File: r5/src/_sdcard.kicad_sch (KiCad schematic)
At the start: 6 parts, among them J14 Micro_SD_Card_Det_JAE_ST11, U10 ESD7004, U11 ESD7004

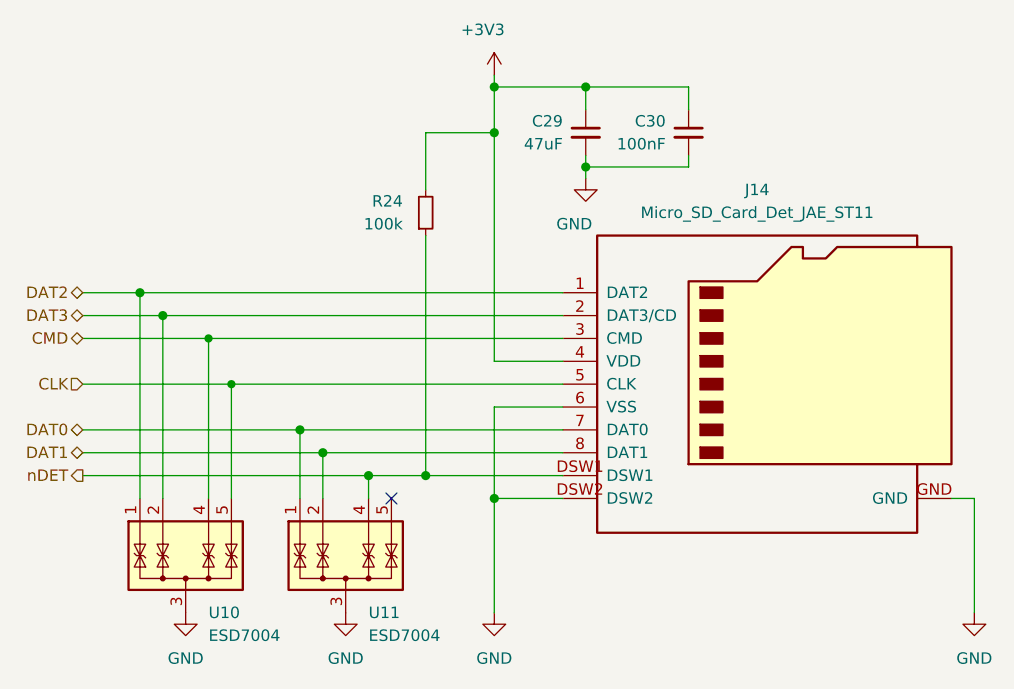
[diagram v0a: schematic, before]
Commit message: Updates to +/-15V supply. Additional output capacitance. Change to smaller inductor packages. Add 0R links to permit isolation of output. Mods to compensation network. Set feedback resistors to datasheet values.
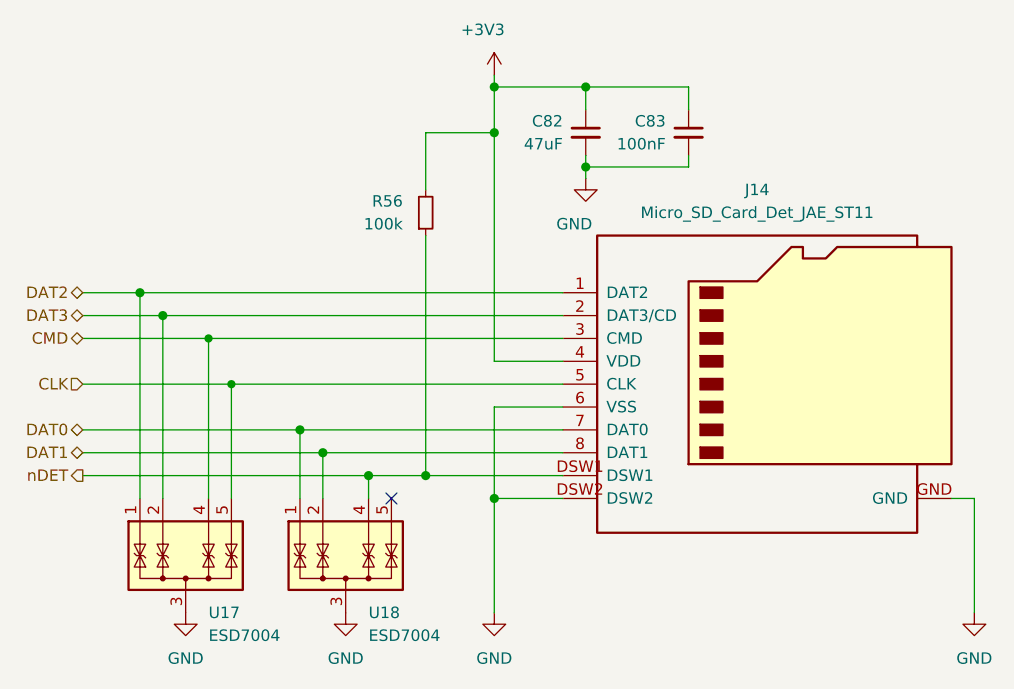
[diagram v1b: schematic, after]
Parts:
- renumbered C29 to C82, C30 to C83, R24 to R56, U10 to U17, U11 to U18
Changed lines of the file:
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@@
   (symbol (lib_id "power:GND") (at 152.4 128.27 0) (unit 1)
     (in_bom yes) (on_board yes) (dnp no)
-    (property "Reference" "#PWR089" (at 152.4 134.62 0)
+    (property "Reference" "#PWR0160" (at 152.4 134.62 0)
       (effects (font (size 1.27 1.27)) hide)
     )
@@
       (project "bugg-main-r5"
         (path "/e3eb514f-6ce4-4abe-ba20-f82f0015628f/498d2354-7ecc-4881-a4b8-afc4730b4589"
-          (reference "#PWR089") (unit 1)
+          (reference "#PWR0160") (unit 1)
         )
       )
@@
   (symbol (lib_id "Device:R_Small") (at 144.78 83.82 0) (mirror x) (unit 1)
     (in_bom yes) (on_board yes) (dnp no)
-    (property "Reference" "R24" (at 142.24 82.55 0)
+    (property "Reference" "R56" (at 142.24 82.55 0)
       (effects (font (size 1.27 1.27)) (justify right))
     )
@@
       (project "bugg-main-r5"
         (path "/e3eb514f-6ce4-4abe-ba20-f82f0015628f/498d2354-7ecc-4881-a4b8-afc4730b4589"
-          (reference "R24") (unit 1)
+          (reference "R56") (unit 1)
         )
       )
@@
   (symbol (lib_id "Device:C_Small") (at 173.99 74.93 0) (mirror y) (unit 1)
     (in_bom yes) (on_board yes) (dnp no)
-    (property "Reference" "C30" (at 171.45 73.66 0)
+    (property "Reference" "C83" (at 171.45 73.66 0)
       (effects (font (size 1.27 1.27)) (justify left))
     )
@@
       (project "bugg-main-r5"
         (path "/e3eb514f-6ce4-4abe-ba20-f82f0015628f/498d2354-7ecc-4881-a4b8-afc4730b4589"
-          (reference "C30") (unit 1)
+          (reference "C83") (unit 1)
         )
       )
@@
   (symbol (lib_id "power:GND") (at 205.74 128.27 0) (unit 1)
     (in_bom yes) (on_board yes) (dnp no)
-    (property "Reference" "#PWR091" (at 205.74 134.62 0)
+    (property "Reference" "#PWR0162" (at 205.74 134.62 0)
       (effects (font (size 1.27 1.27)) hide)
     )
@@
       (project "bugg-main-r5"
         (path "/e3eb514f-6ce4-4abe-ba20-f82f0015628f/498d2354-7ecc-4881-a4b8-afc4730b4589"
-          (reference "#PWR091") (unit 1)
+          (reference "#PWR0162") (unit 1)
         )
       )
@@
   (symbol (lib_id "Device:C_Small") (at 162.56 74.93 0) (mirror y) (unit 1)
     (in_bom yes) (on_board yes) (dnp no)
-    (property "Reference" "C29" (at 160.02 73.66 0)
+    (property "Reference" "C82" (at 160.02 73.66 0)
       (effects (font (size 1.27 1.27)) (justify left))
     )
@@
       (project "bugg-main-r5"
         (path "/e3eb514f-6ce4-4abe-ba20-f82f0015628f/498d2354-7ecc-4881-a4b8-afc4730b4589"
-          (reference "C29") (unit 1)
+          (reference "C82") (unit 1)
         )
       )
@@
   (symbol (lib_id "power:GND") (at 118.11 128.27 0) (unit 1)
     (in_bom yes) (on_board yes) (dnp no)
-    (property "Reference" "#PWR086" (at 118.11 134.62 0)
+    (property "Reference" "#PWR0157" (at 118.11 134.62 0)
       (effects (font (size 1.27 1.27)) hide)
     )
@@
       (project "bugg-main-r5"
         (path "/e3eb514f-6ce4-4abe-ba20-f82f0015628f/498d2354-7ecc-4881-a4b8-afc4730b4589"
-          (reference "#PWR086") (unit 1)
+          (reference "#PWR0157") (unit 1)
         )
       )
@@
   (symbol (lib_id "power:GND") (at 162.56 80.01 0) (mirror y) (unit 1)
     (in_bom yes) (on_board yes) (dnp no)
-    (property "Reference" "#PWR090" (at 162.56 86.36 0)
+    (property "Reference" "#PWR0161" (at 162.56 86.36 0)
       (effects (font (size 1.27 1.27)) hide)
     )
@@
       (project "bugg-main-r5"
         (path "/e3eb514f-6ce4-4abe-ba20-f82f0015628f/498d2354-7ecc-4881-a4b8-afc4730b4589"
-          (reference "#PWR090") (unit 1)
+          (reference "#PWR0161") (unit 1)
         )
       )
@@
   (symbol (lib_id "j_Power_Protection:ESD7004") (at 118.11 123.19 0) (unit 1)
     (in_bom yes) (on_board yes) (dnp no)
-    (property "Reference" "U10" (at 120.65 128.27 0)
+    (property "Reference" "U17" (at 120.65 128.27 0)
       (effects (font (size 1.27 1.27)) (justify left))
     )
@@
       (project "bugg-main-r5"
         (path "/e3eb514f-6ce4-4abe-ba20-f82f0015628f/498d2354-7ecc-4881-a4b8-afc4730b4589"
-          (reference "U10") (unit 1)
+          (reference "U17") (unit 1)
         )
       )
@@
   (symbol (lib_id "power:+3V3") (at 152.4 68.58 0) (mirror y) (unit 1)
     (in_bom yes) (on_board yes) (dnp no)
-    (property "Reference" "#PWR088" (at 152.4 72.39 0)
+    (property "Reference" "#PWR0159" (at 152.4 72.39 0)
       (effects (font (size 1.27 1.27)) hide)
     )
@@
       (project "bugg-main-r5"
         (path "/e3eb514f-6ce4-4abe-ba20-f82f0015628f/498d2354-7ecc-4881-a4b8-afc4730b4589"
-          (reference "#PWR088") (unit 1)
+          (reference "#PWR0159") (unit 1)
         )
       )
@@
   (symbol (lib_id "j_Power_Protection:ESD7004") (at 135.89 123.19 0) (unit 1)
     (in_bom yes) (on_board yes) (dnp no)
-    (property "Reference" "U11" (at 138.43 128.27 0)
+    (property "Reference" "U18" (at 138.43 128.27 0)
       (effects (font (size 1.27 1.27)) (justify left))
     )
@@
       (project "bugg-main-r5"
         (path "/e3eb514f-6ce4-4abe-ba20-f82f0015628f/498d2354-7ecc-4881-a4b8-afc4730b4589"
-          (reference "U11") (unit 1)
+          (reference "U18") (unit 1)
         )
       )
@@
   (symbol (lib_id "power:GND") (at 135.89 128.27 0) (unit 1)
     (in_bom yes) (on_board yes) (dnp no)
-    (property "Reference" "#PWR087" (at 135.89 134.62 0)
+    (property "Reference" "#PWR0158" (at 135.89 134.62 0)
       (effects (font (size 1.27 1.27)) hide)
     )
@@
       (project "bugg-main-r5"
         (path "/e3eb514f-6ce4-4abe-ba20-f82f0015628f/498d2354-7ecc-4881-a4b8-afc4730b4589"
-          (reference "#PWR087") (unit 1)
-        )
-      )
+          (reference "#PWR0158") (unit 1)
+        )
+      )

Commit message: Fix broken component annotation by importing back from PCB and fixing duplicates.
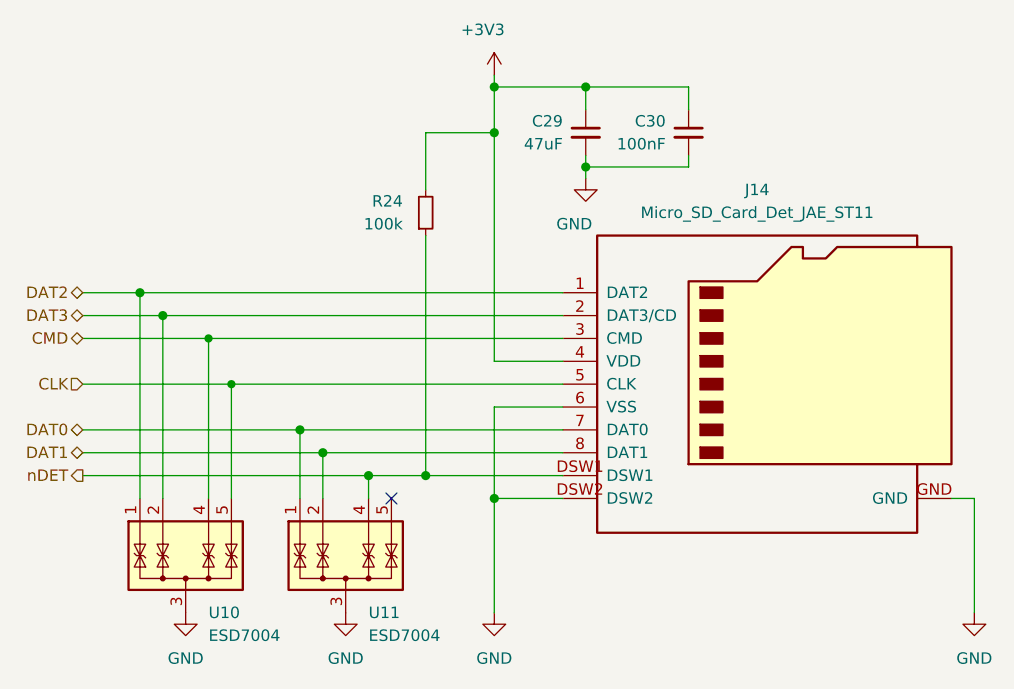
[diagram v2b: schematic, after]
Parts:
- renumbered C82 to C29, C83 to C30, R56 to R24, U17 to U10, U18 to U11
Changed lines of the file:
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@@
   (symbol (lib_id "Device:R_Small") (at 144.78 83.82 0) (mirror x) (unit 1)
     (in_bom yes) (on_board yes) (dnp no)
-    (property "Reference" "R56" (at 142.24 82.55 0)
+    (property "Reference" "R24" (at 142.24 82.55 0)
       (effects (font (size 1.27 1.27)) (justify right))
     )
@@
       (project "bugg-main-r5"
         (path "/e3eb514f-6ce4-4abe-ba20-f82f0015628f/498d2354-7ecc-4881-a4b8-afc4730b4589"
-          (reference "R56") (unit 1)
+          (reference "R24") (unit 1)
         )
       )
@@
   (symbol (lib_id "Device:C_Small") (at 173.99 74.93 0) (mirror y) (unit 1)
     (in_bom yes) (on_board yes) (dnp no)
-    (property "Reference" "C83" (at 171.45 73.66 0)
+    (property "Reference" "C30" (at 171.45 73.66 0)
       (effects (font (size 1.27 1.27)) (justify left))
     )
@@
       (project "bugg-main-r5"
         (path "/e3eb514f-6ce4-4abe-ba20-f82f0015628f/498d2354-7ecc-4881-a4b8-afc4730b4589"
-          (reference "C83") (unit 1)
+          (reference "C30") (unit 1)
         )
       )
@@
   (symbol (lib_id "Device:C_Small") (at 162.56 74.93 0) (mirror y) (unit 1)
     (in_bom yes) (on_board yes) (dnp no)
-    (property "Reference" "C82" (at 160.02 73.66 0)
+    (property "Reference" "C29" (at 160.02 73.66 0)
       (effects (font (size 1.27 1.27)) (justify left))
     )
@@
       (project "bugg-main-r5"
         (path "/e3eb514f-6ce4-4abe-ba20-f82f0015628f/498d2354-7ecc-4881-a4b8-afc4730b4589"
-          (reference "C82") (unit 1)
+          (reference "C29") (unit 1)
         )
       )
@@
   (symbol (lib_id "j_Power_Protection:ESD7004") (at 118.11 123.19 0) (unit 1)
     (in_bom yes) (on_board yes) (dnp no)
-    (property "Reference" "U17" (at 120.65 128.27 0)
+    (property "Reference" "U10" (at 120.65 128.27 0)
       (effects (font (size 1.27 1.27)) (justify left))
     )
@@
       (project "bugg-main-r5"
         (path "/e3eb514f-6ce4-4abe-ba20-f82f0015628f/498d2354-7ecc-4881-a4b8-afc4730b4589"
-          (reference "U17") (unit 1)
+          (reference "U10") (unit 1)
         )
       )
@@
   (symbol (lib_id "j_Power_Protection:ESD7004") (at 135.89 123.19 0) (unit 1)
     (in_bom yes) (on_board yes) (dnp no)
-    (property "Reference" "U18" (at 138.43 128.27 0)
+    (property "Reference" "U11" (at 138.43 128.27 0)
       (effects (font (size 1.27 1.27)) (justify left))
     )
@@
       (project "bugg-main-r5"
         (path "/e3eb514f-6ce4-4abe-ba20-f82f0015628f/498d2354-7ecc-4881-a4b8-afc4730b4589"
-          (reference "U18") (unit 1)
-        )
-      )
+          (reference "U11") (unit 1)
+        )
+      )

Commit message: Update layout to standardise on 0402 passives everywhere possible. This reduces the number of BoM lines. DRC passed. Add DRC exclusions for unavoidable violations
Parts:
- C30: footprint Capacitor_SMD:C_0603_1608Metric -> Capacitor_SMD:C_0402_1005Metric
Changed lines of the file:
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@@
       (effects (font (size 1.27 1.27)) (justify left))
     )
-    (property "Footprint" "Capacitor_SMD:C_0603_1608Metric" (at 173.99 74.93 0)
+    (property "Footprint" "Capacitor_SMD:C_0402_1005Metric" (at 173.99 74.93 0)
       (effects (font (size 1.27 1.27)) hide)
     )

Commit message: Change 0805 47uF to 1206 to save a BOM line. Update layout, DRC pass.
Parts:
- C29: footprint Capacitor_SMD:C_0805_2012Metric -> Capacitor_SMD:C_1206_3216Metric
- C30: MPN (none) -> GRM155R71H104KE14D; Manufacturer (none) -> Murata; Mouser (none) -> 81-GRM155R71H104KE4D; Voltage (none) -> 50V
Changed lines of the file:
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@@
+      (effects (font (size 1.27 1.27)) hide)
+    )
+    (property "Digikey" "" (at 182.88 102.87 0)
+      (effects (font (size 1.27 1.27)) hide)
+    )
+    (property "MPN" "" (at 182.88 102.87 0)
+      (effects (font (size 1.27 1.27)) hide)
+    )
+    (property "Mouser" "" (at 182.88 102.87 0)
+      (effects (font (size 1.27 1.27)) hide)
+    )
+    (property "Field-1" "" (at 182.88 102.87 0)
       (effects (font (size 1.27 1.27)) hide)
     )
@@
       (effects (font (size 1.27 1.27)) hide)
     )
+    (property "Digikey" "" (at 144.78 83.82 0)
+      (effects (font (size 1.27 1.27)) hide)
+    )
+    (property "MPN" "" (at 144.78 83.82 0)
+      (effects (font (size 1.27 1.27)) hide)
+    )
+    (property "Mouser" "" (at 144.78 83.82 0)
+      (effects (font (size 1.27 1.27)) hide)
+    )
+    (property "Field-1" "" (at 144.78 83.82 0)
+      (effects (font (size 1.27 1.27)) hide)
+    )
     (pin "1")
     (pin "2")
@@
       (effects (font (size 1.27 1.27)) hide)
     )
+    (property "Digikey" "" (at 173.99 74.93 0)
+      (effects (font (size 1.27 1.27)) hide)
+    )
+    (property "MPN" "GRM155R71H104KE14D " (at 173.99 74.93 0)
+      (effects (font (size 1.27 1.27)) hide)
+    )
+    (property "Mouser" "81-GRM155R71H104KE4D " (at 173.99 74.93 0)
+      (effects (font (size 1.27 1.27)) hide)
+    )
+    (property "Field-1" "" (at 173.99 74.93 0)
+      (effects (font (size 1.27 1.27)) hide)
+    )
+    (property "Manufacturer" "Murata" (at 173.99 74.93 0)
+      (effects (font (size 1.27 1.27)) hide)
+    )
+    (property "Voltage" "50V" (at 173.99 74.93 0)
+      (effects (font (size 1.27 1.27)) hide)
+    )
     (pin "1")
     (pin "2")
@@
       (effects (font (size 1.27 1.27)) (justify left))
     )
-    (property "Footprint" "Capacitor_SMD:C_0805_2012Metric" (at 162.56 74.93 0)
+    (property "Footprint" "Capacitor_SMD:C_1206_3216Metric" (at 162.56 74.93 0)
       (effects (font (size 1.27 1.27)) hide)
     )
@@
     )
     (property "Quantity" "" (at 162.56 74.93 0)
+      (effects (font (size 1.27 1.27)) hide)
+    )
+    (property "Digikey" "" (at 162.56 74.93 0)
+      (effects (font (size 1.27 1.27)) hide)
+    )
+    (property "MPN" "" (at 162.56 74.93 0)
+      (effects (font (size 1.27 1.27)) hide)
+    )
+    (property "Mouser" "" (at 162.56 74.93 0)
+      (effects (font (size 1.27 1.27)) hide)
+    )
+    (property "Field-1" "" (at 162.56 74.93 0)
       (effects (font (size 1.27 1.27)) hide)
     )
@@
     )
     (property "Quantity" "" (at 118.11 123.19 0)
+      (effects (font (size 1.27 1.27)) hide)
+    )
+    (property "Digikey" "" (at 118.11 123.19 0)
+      (effects (font (size 1.27 1.27)) hide)
+    )
+    (property "MPN" "" (at 118.11 123.19 0)
+      (effects (font (size 1.27 1.27)) hide)
+    )
+    (property "Mouser" "" (at 118.11 123.19 0)
+      (effects (font (size 1.27 1.27)) hide)
+    )
+    (property "Field-1" "" (at 118.11 123.19 0)
       (effects (font (size 1.27 1.27)) hide)
     )
@@
       (effects (font (size 1.27 1.27)) hide)
     )
+    (property "Digikey" "" (at 135.89 123.19 0)
+      (effects (font (size 1.27 1.27)) hide)
+    )
+    (property "MPN" "" (at 135.89 123.19 0)
+      (effects (font (size 1.27 1.27)) hide)
+    )
+    (property "Mouser" "" (at 135.89 123.19 0)
+      (effects (font (size 1.27 1.27)) hide)
+    )
+    (property "Field-1" "" (at 135.89 123.19 0)
+      (effects (font (size 1.27 1.27)) hide)
+    )
